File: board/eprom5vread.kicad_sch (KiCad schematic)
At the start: 0 parts

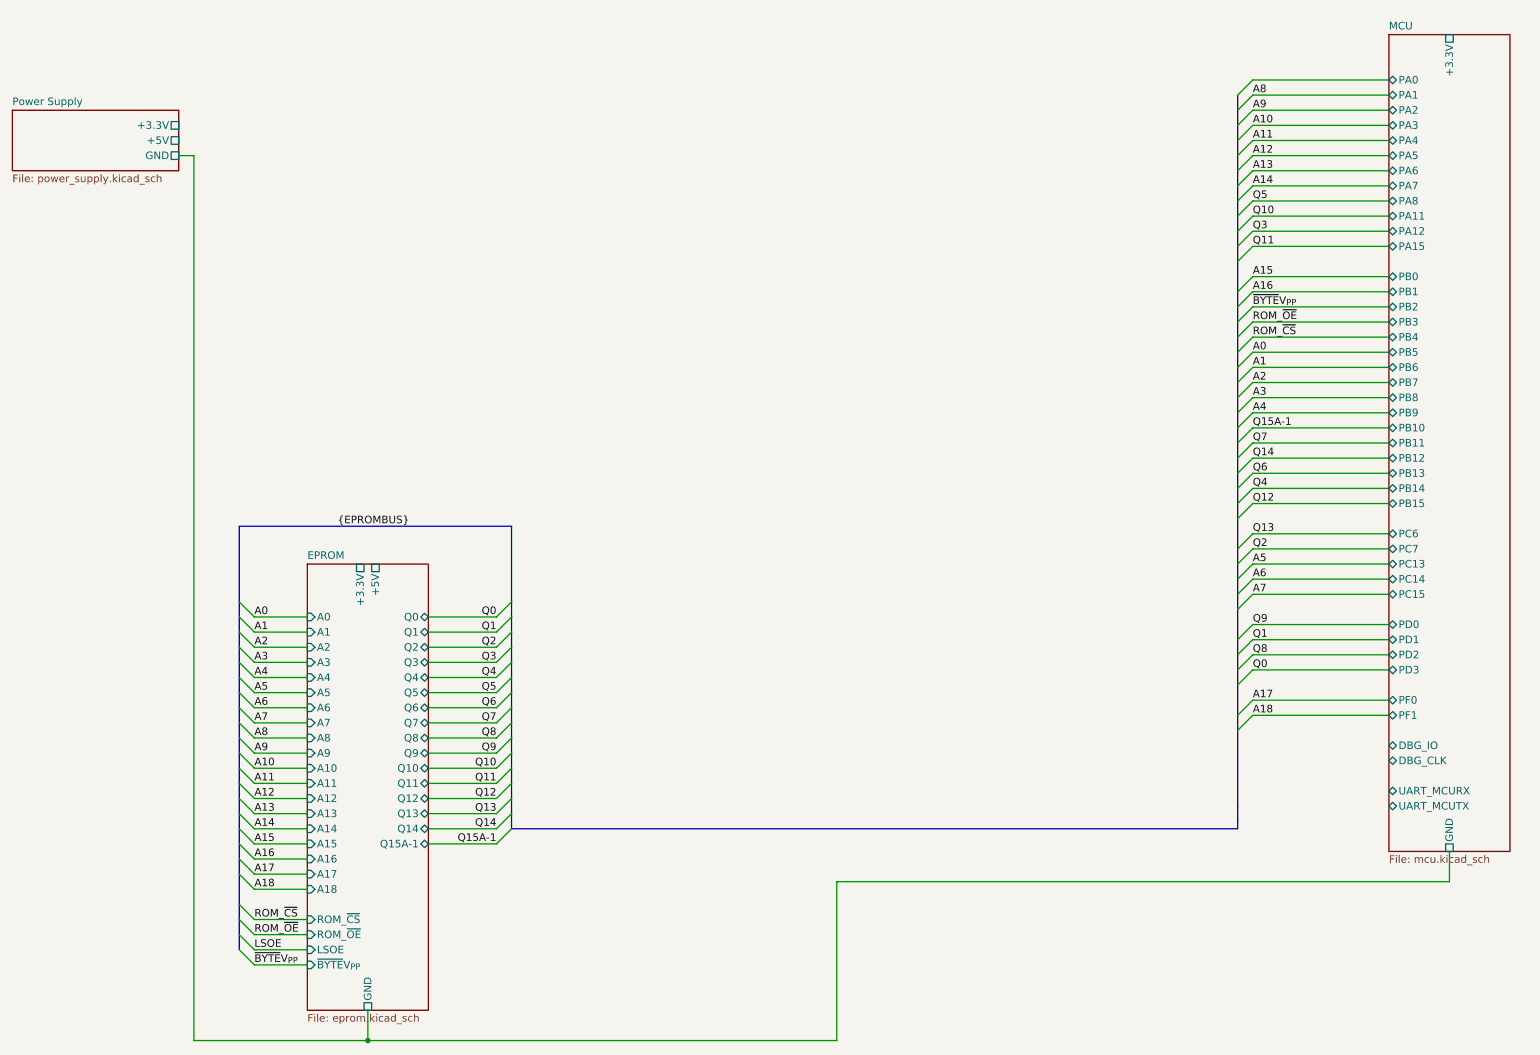
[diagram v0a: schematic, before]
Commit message: initial board layout (WIP), schematic tuning
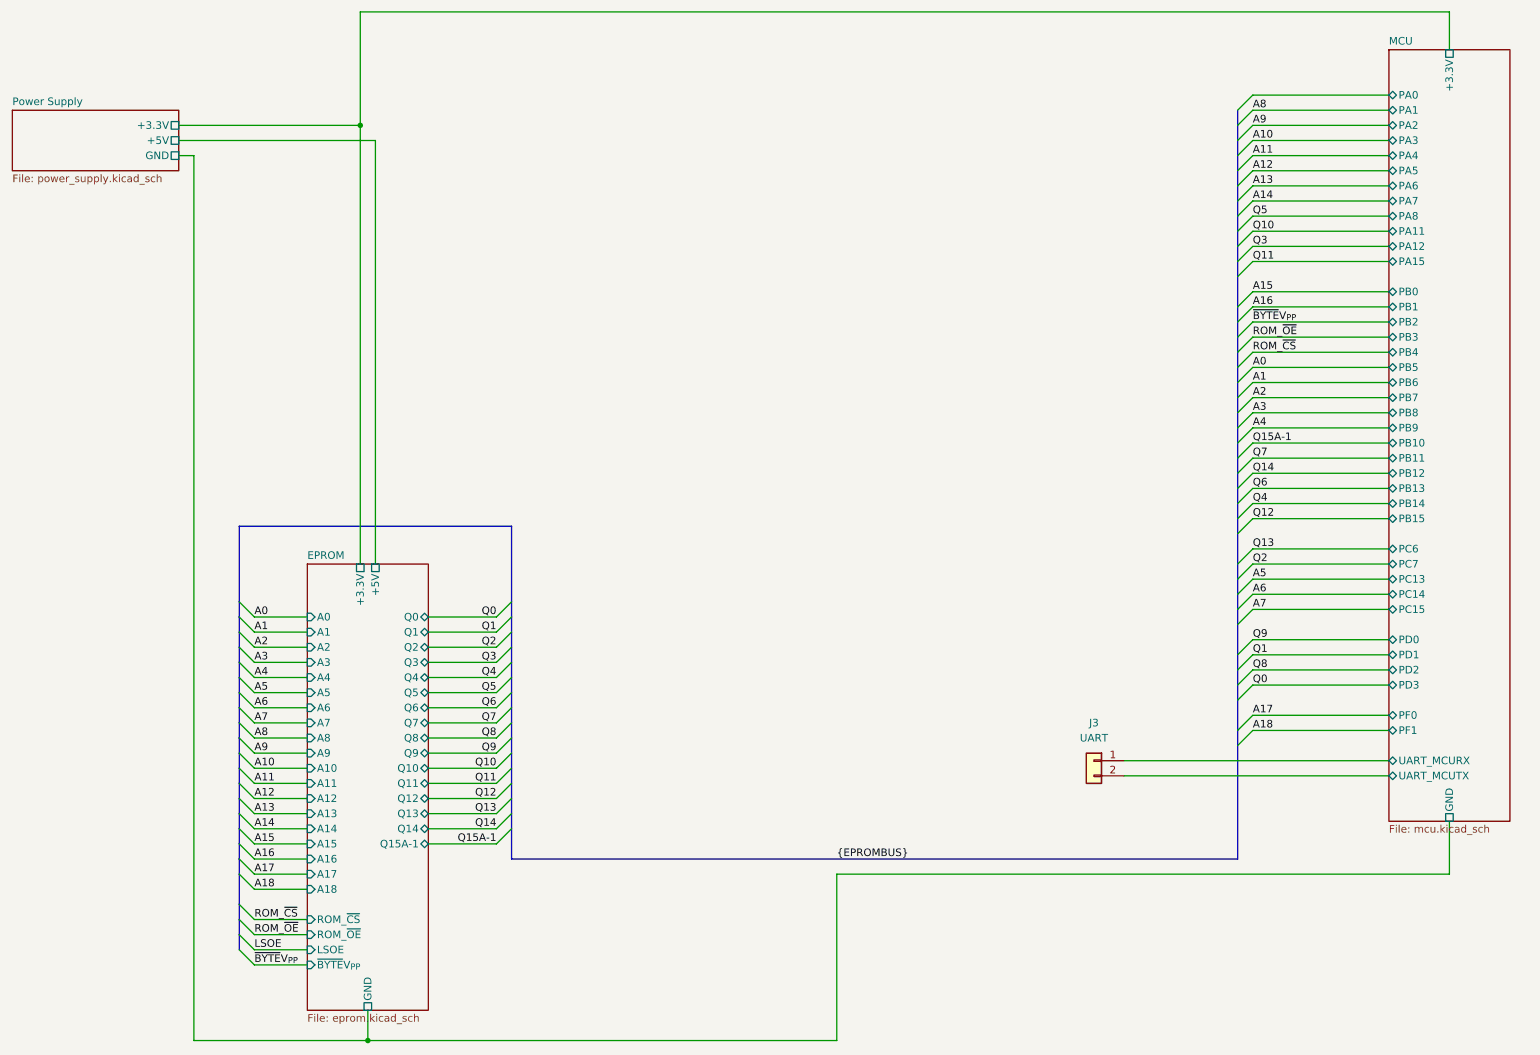
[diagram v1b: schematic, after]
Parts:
- added J3: UART, Connector_PinHeader_2.54mm:PinHeader_2x01_P2.54mm_Vertical_SMD, symbol Connector_Generic:Conn_01x02
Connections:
- net MCU/UART_MCURX: now also J3.1 (Pin_1)
- net MCU/UART_MCUTX: now also J3.2 (Pin_2)
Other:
- sheet MCU ports: added none; removed DBG_CLK, DBG_IO

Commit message: finish board design
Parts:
- renumbered J3 to J102
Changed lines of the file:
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@@
   (paper "A4")
   (bus_alias "EPROMBUS" (members "A[0..18]" "Q[0..14]" "Q15A-1" "ROM_~{CS}" "ROM_~{OE}" "LSOE" "~{BYTE}V_{PP}"))
-  (bus_alias "MCUPWR" (members "VDD" "VBAT" "VREF+" "VSS"))
+  (bus_alias "MCUPWR" (members "VDD" "VBAT" "VREF+" "GND"))
   (junction (at 85.09 186.69) (diameter 0) (color 0 0 0 0)
   )
@@
   )
   (label "A6" (at 66.04 130.81 0) (fields_autoplaced)
+    (effects (font (size 1.27 1.27)) (justify left bottom))
+  )
+  (label "LSOE" (at 233.68 27.94 0) (fields_autoplaced)
     (effects (font (size 1.27 1.27)) (justify left bottom))
   )
@@
   (symbol (lib_id "Connector_Generic:Conn_01x02") (at 207.01 139.7 0) (mirror y) (unit 1)
     (in_bom yes) (on_board yes) (dnp no) (fields_autoplaced)
-    (property "Reference" "J3" (at 207.01 133.35 0)
+    (property "Reference" "J102" (at 207.01 133.35 0)
       (effects (font (size 1.27 1.27)))
     )
@@
       (project "eprom5vread"
         (path "/b08a8275-42d3-43c1-b04c-f89506e7527b"
-          (reference "J3") (unit 1)
+          (reference "J102") (unit 1)
         )
       )

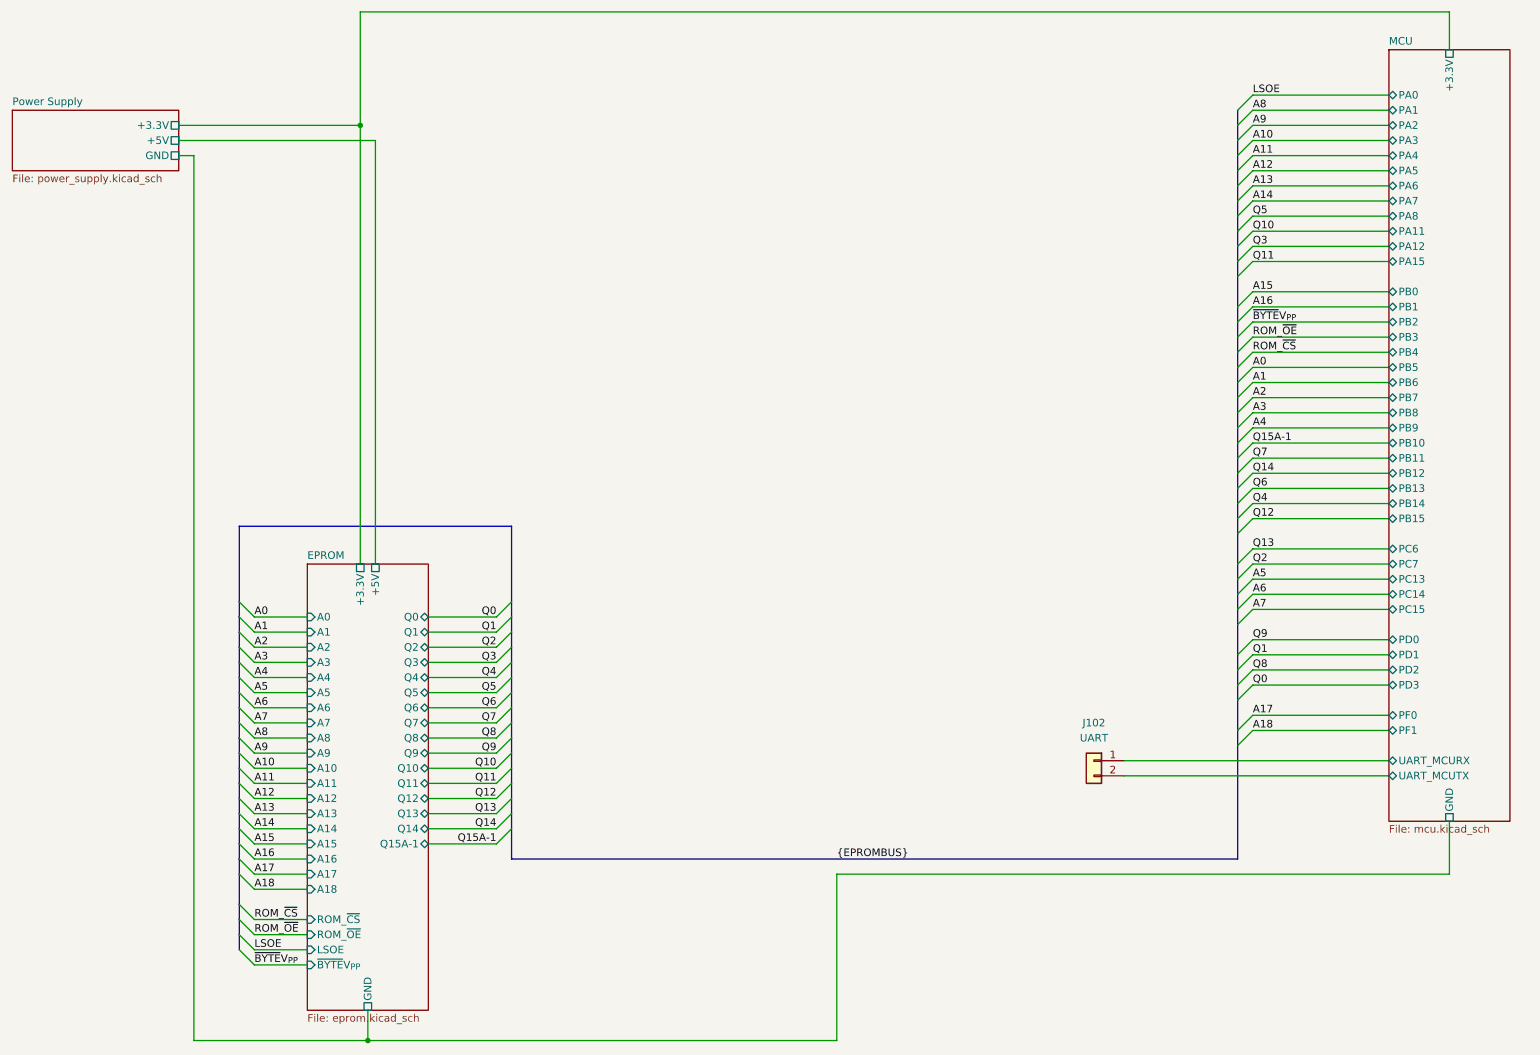
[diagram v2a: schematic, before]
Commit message: redo board to use I2C port expanders (and smaller MCU)
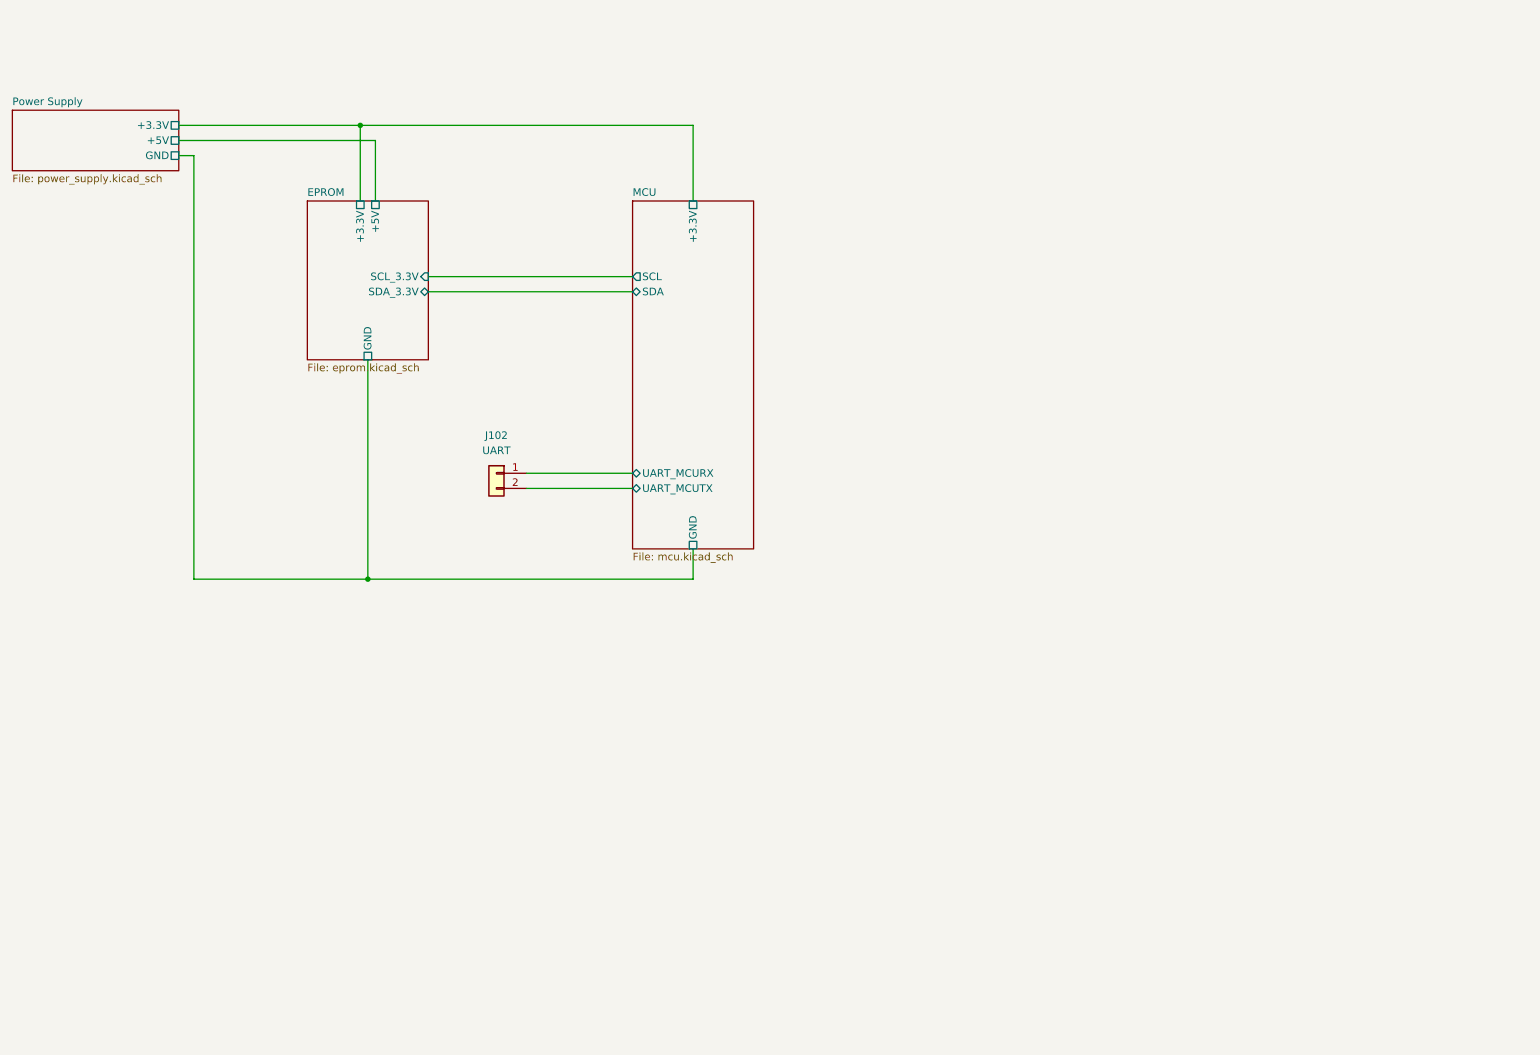
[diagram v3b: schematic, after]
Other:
- sheet EPROM ports: added SCL_3.3V, SDA_3.3V; removed A0, A1, A10, A11, A12, A13, A14, A15, A16, A17, A18, A2, A3, A4, A5, A6, A7, A8, A9, LSOE, Q0, Q1, Q10, Q11, Q12, Q13, Q14, Q15A-1, Q2, Q3, Q4, Q5, Q6, Q7, Q8, Q9, ROM_~{CS}, ROM_~{OE}, ~{BYTE}V_{PP}
- sheet MCU ports: added SCL, SDA; removed PA0, PA1, PA11, PA12, PA15, PA2, PA3, PA4, PA5, PA6, PA7, PA8, PB0, PB1, PB10, PB11, PB12, PB13, PB14, PB15, PB2, PB3, PB4, PB5, PB6, PB7, PB8, PB9, PC13, PC14, PC15, PC6, PC7, PD0, PD1, PD2, PD3, PF0, PF1
- moved on the sheet: J102

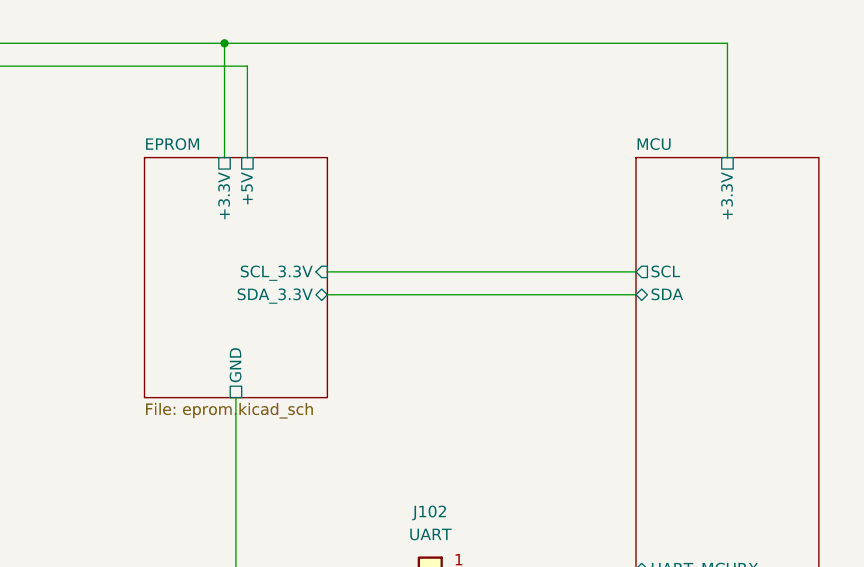
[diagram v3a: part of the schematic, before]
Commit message: allow driving ~RESET pins of I2C I/O expanders, add missing resistors
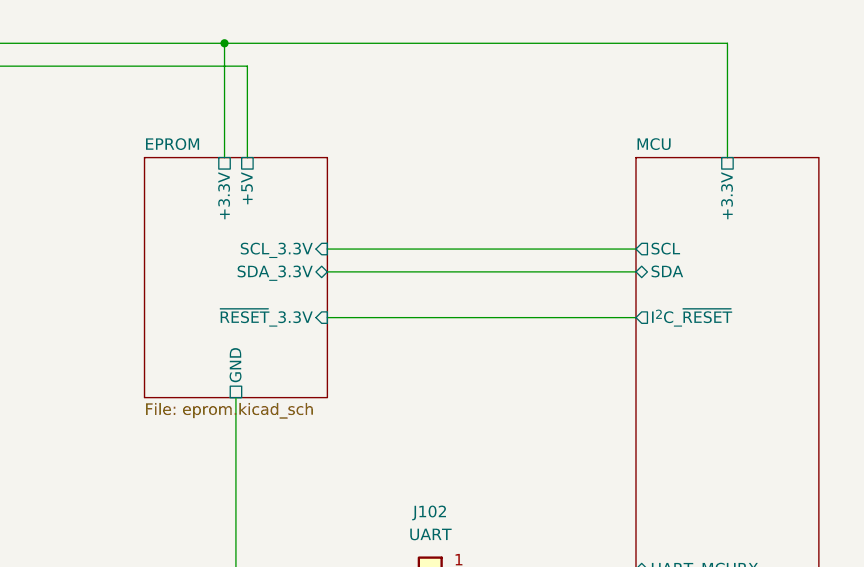
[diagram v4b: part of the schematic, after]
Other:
- sheet EPROM ports: added ~{RESET}_3.3V; removed none
- sheet MCU ports: added I^{2}C_~{RESET}; removed none
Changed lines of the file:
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@@
+	(wire
+		(pts
+			(xy 95.25 63.5) (xy 129.54 63.5)
+		)
+		(stroke
+			(width 0)
+			(type default)
+		)
+	)
 	(wire
 		(pts
@@
 	(wire
 		(pts
-			(xy 95.25 60.96) (xy 129.54 60.96)
+			(xy 95.25 55.88) (xy 129.54 55.88)
 		)
 		(stroke
@@
 		)
 		(pin "SCL" output
+			(at 129.54 55.88 180)
+			(effects
+				(font
+					(size 1.27 1.27)
+				)
+				(justify left)
+			)
+		)
+		(pin "SDA" bidirectional
 			(at 129.54 58.42 180)
 			(effects
@@
 			)
 		)
-		(pin "SDA" bidirectional
-			(at 129.54 60.96 180)
+		(pin "I^{2}C_~{RESET}" output
+			(at 129.54 63.5 180)
 			(effects
 				(font
@@
 		)
 		(pin "SCL_3.3V" input
+			(at 95.25 55.88 0)
+			(effects
+				(font
+					(size 1.27 1.27)
+				)
+				(justify right)
+			)
+		)
+		(pin "SDA_3.3V" bidirectional
 			(at 95.25 58.42 0)
 			(effects
@@
 			)
 		)
-		(pin "SDA_3.3V" bidirectional
-			(at 95.25 60.96 0)
-			(effects
-				(font
+		(pin "~{RESET}_3.3V" input
+			(at 95.25 63.5 0)
+			(effects
+				(font
